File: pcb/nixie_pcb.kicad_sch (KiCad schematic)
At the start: 8 parts

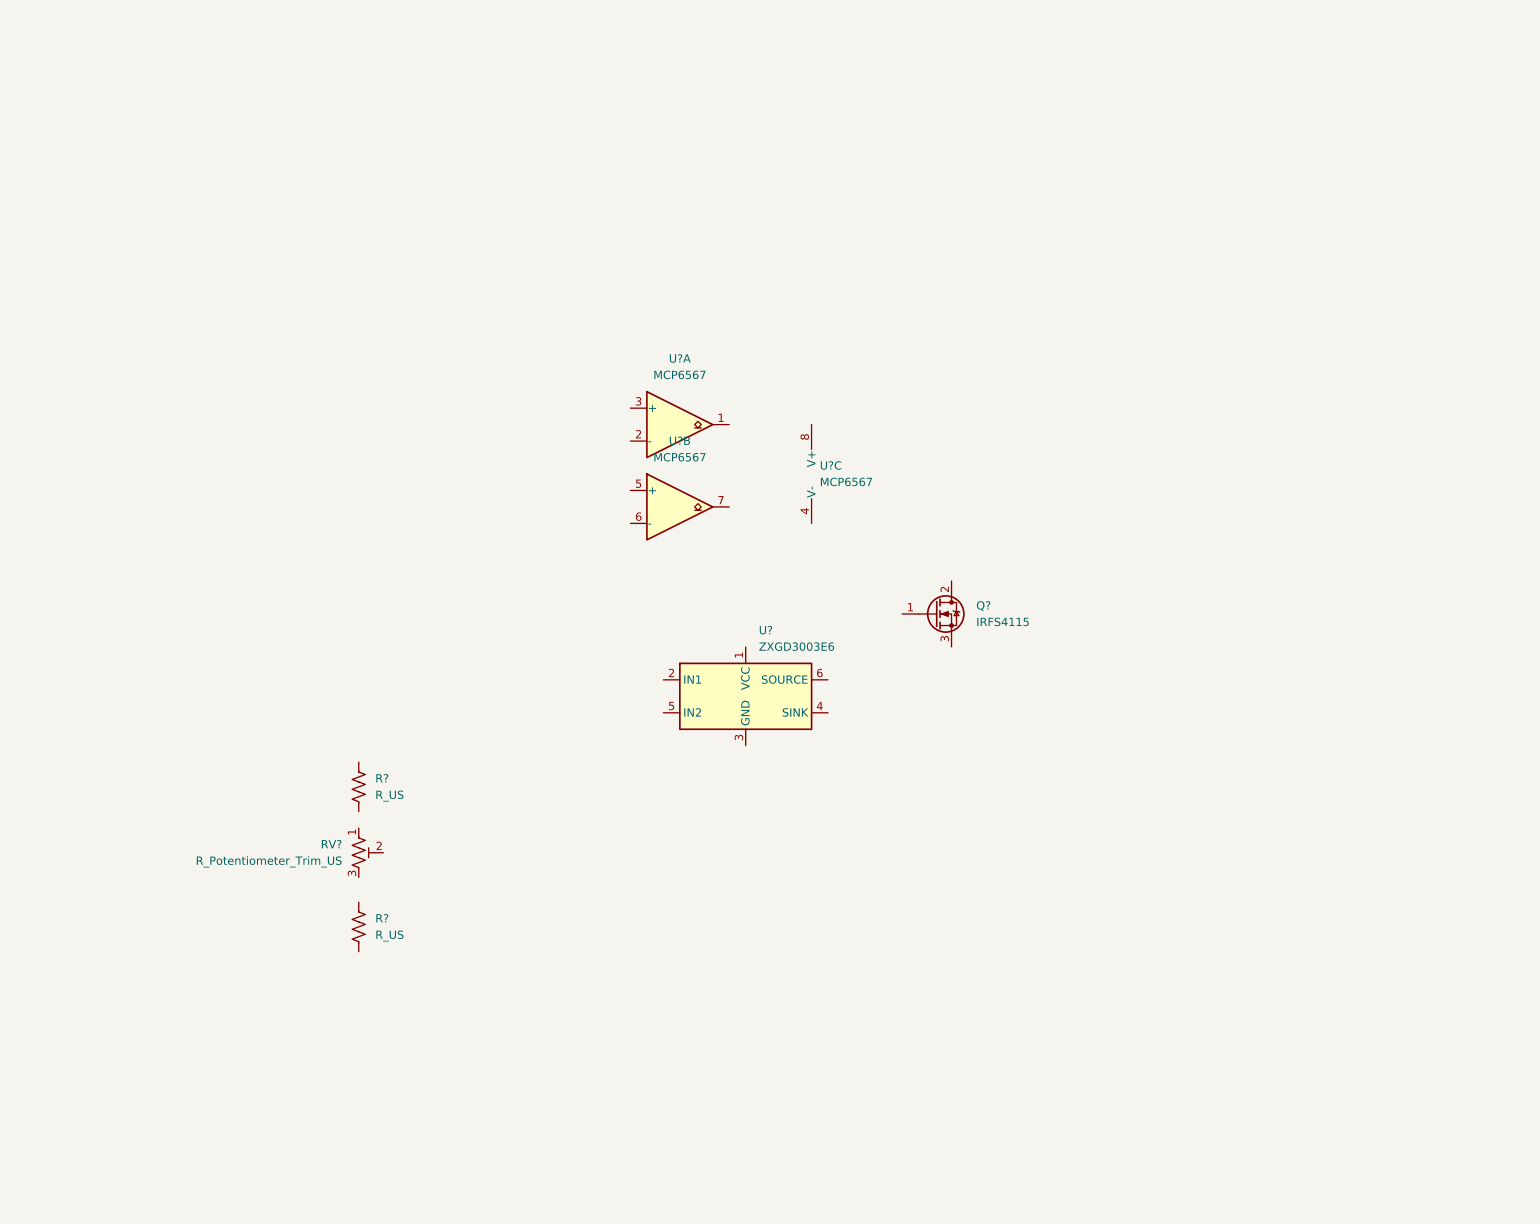
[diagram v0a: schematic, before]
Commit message: Schem from ltspice to kicad
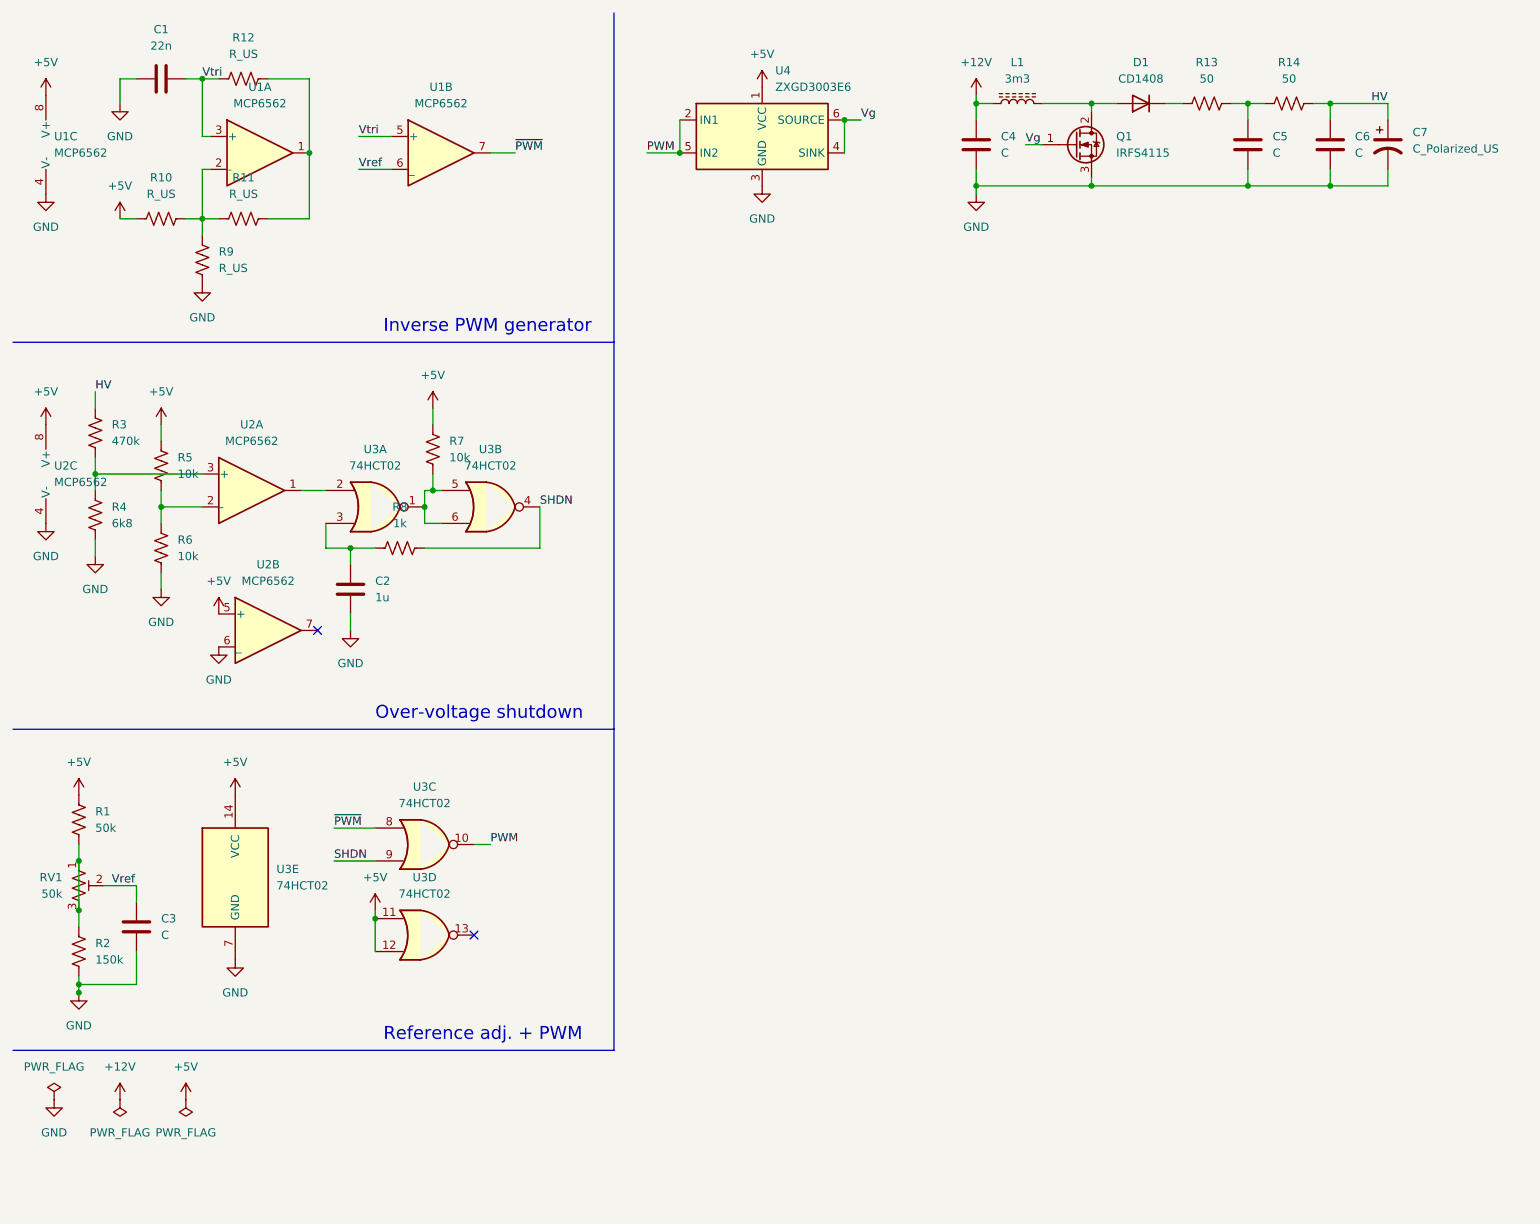
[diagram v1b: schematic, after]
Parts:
- removed U? (x3): MCP6567, symbol Comparator:MCP6567
- added C1: 22n, symbol Device:C
- added C2: 1u, symbol Device:C
- added C3, C4, C5, C6: C, symbol Device:C
- added C7: C_Polarized_US, symbol Device:C_Polarized_US
- added D1: CD1408, Diode_SMD:D_SOD-123, symbol Diode:1N4001
- added L1: 3m3, symbol Device:L_Ferrite
- added R10, R11, R12, R9: R_US, symbol Device:R_US
- added R13, R14: 50, symbol Device:R_US
- added R3: 470k, symbol Device:R_US
- added R4: 6k8, symbol Device:R_US
- added R5, R6, R7: 10k, symbol Device:R_US
- added R8: 1k, symbol Device:R_US
- added U1, U2: MCP6562, symbol custom_parts:MCP6562
- added U3: 74HCT02, symbol 74xx:74HCT02
- R1: renamed from R?; value R_US -> 50k
- R2: renamed from R?; value R_US -> 150k
- RV1: renamed from RV?; value R_Potentiometer_Trim_US -> 50k; footprint (none) -> Potentiometer_SMD:Potentiometer_Bourns_TC33X_Vertical
- gave numbers to parts that had none: 2
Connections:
- net at RV1.1: now also R1.2, R2.1, RV1.3
- net Vref: now reaches RV1.2
- net Vref: now also C3.1, U1.6 (_)
- net GND: now reaches R2.2
- net GND: now also Q1.3 (S), U4.3 (GND), C1.1, C2.2, C3.2, C4.2, C5.2, C6.2, C7.2, R4.2, R6.2, R9.2, U1.4 (V-), U2.4 (V-), U2.6 (_), U3.7 (GND)
- net +5V: now reaches U4.1 (VCC)
- net +5V: now also R1.1, R10.1, R5.1, R7.1, U1.8 (V+), U2.5 (+), U2.8 (V+), U3.11, U3.12, U3.14 (VCC)
- net PWM: now reaches U4.2 (IN1)
- net PWM: now also U4.5 (IN2), U3.10
- net Vg: now reaches U4.4 (SINK)
- net Vg: now also Q1.1 (G), U4.6 (SOURCE)
- net at Q1.2 (D): now also D1.2 (A), L1.2
- new net: R7.2, U3.1, U3.5, U3.6
- new net: U2.1, U3.2
- new net: C2.1, R8.1, U3.3
- new net: D1.1 (K), R13.1
- new net: C5.1, R13.2, R14.1
- new net: R11.1, R12.2, U1.1
- new net: R10.2, R11.2, R9.1, U1.2 (-)
- new net: R3.2, R4.1, U2.3 (+)
- new net: R5.2, R6.1, U2.2 (-)
- new net +12V: C4.1, L1.1
- new net HV: C6.1, C7.1, R14.2, R3.1
- new net SHDN: R8.2, U3.4, U3.9
- new net Vtri: C1.2, R12.1, U1.3 (+), U1.5 (+)
- new net ~{PWM}: U1.7, U3.8
- no-connect marks 0 -> 2
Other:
- note added: "Inverse PWM generator"
- note added: "Over-voltage shutdown"
- note added: "Reference adj. + PWM"
- title: (none) -> Nixie tube PSU
- moved on the sheet: Q1, R1, R2, RV1, U4

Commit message: save
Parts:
- added U5: AP7370-50W5-7, custom_parts:SOT95P285X140-5N, symbol custom_parts:AP7370-50W5-7
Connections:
- net +12V: now also U5.1 (VIN)
- net +5V: now also U5.5 (VOUT)
- net GND: now also U5.2 (GND)
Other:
- note added: "Power"
- moved on the sheet: C4, C5, C6, C7, D1, L1, Q1, R13, R14
